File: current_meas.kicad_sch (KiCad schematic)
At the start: 33 parts, among them U23 LT3060ETS8-5#TRMPBF, U24 INA180A2IDBVR, U25 INA180A2IDBVR

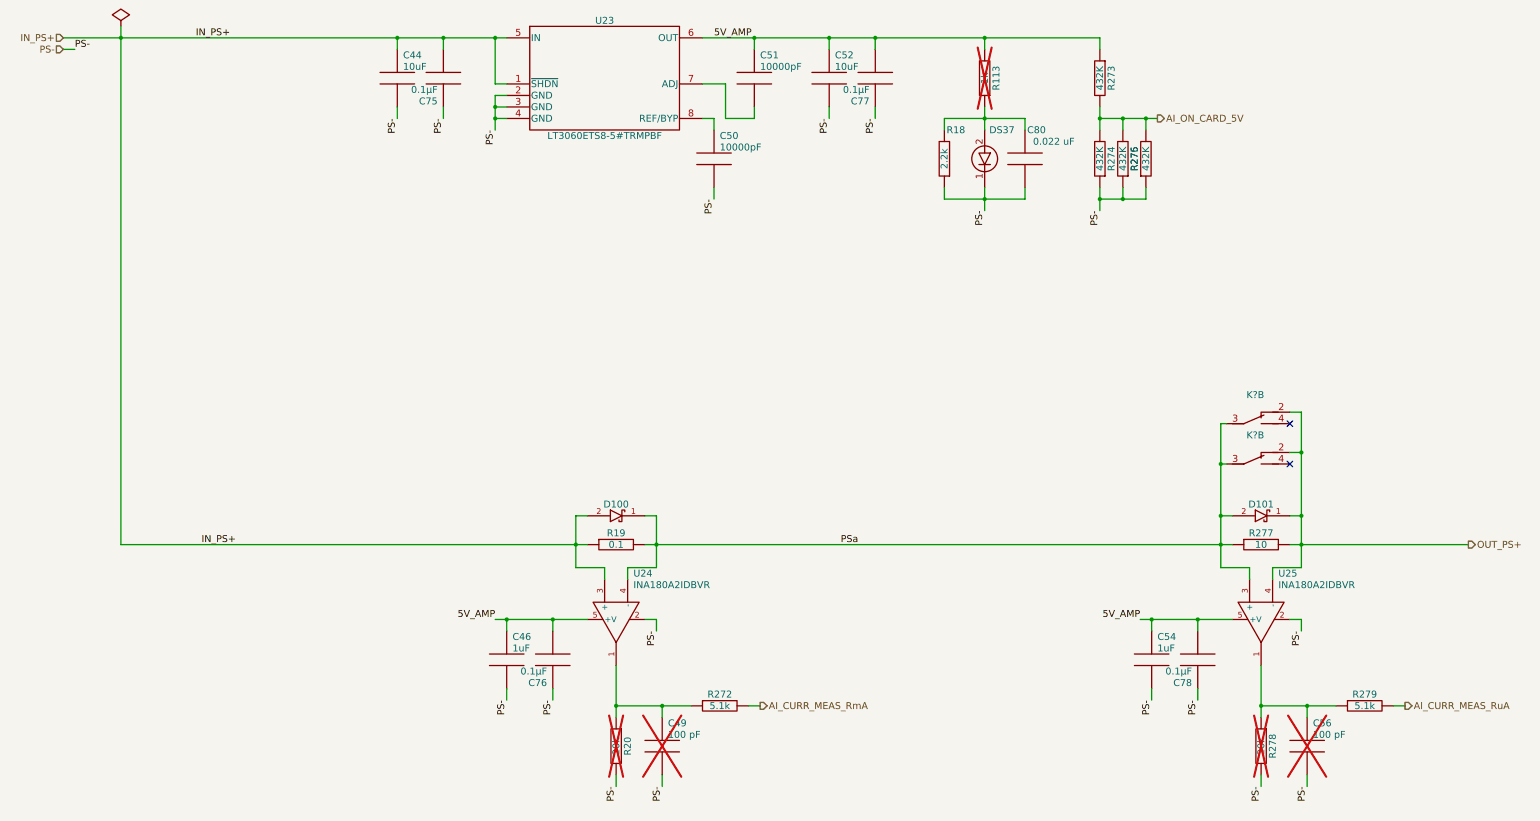
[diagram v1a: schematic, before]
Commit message: kicad 9 - r11-check gerber before sending to manufacturing
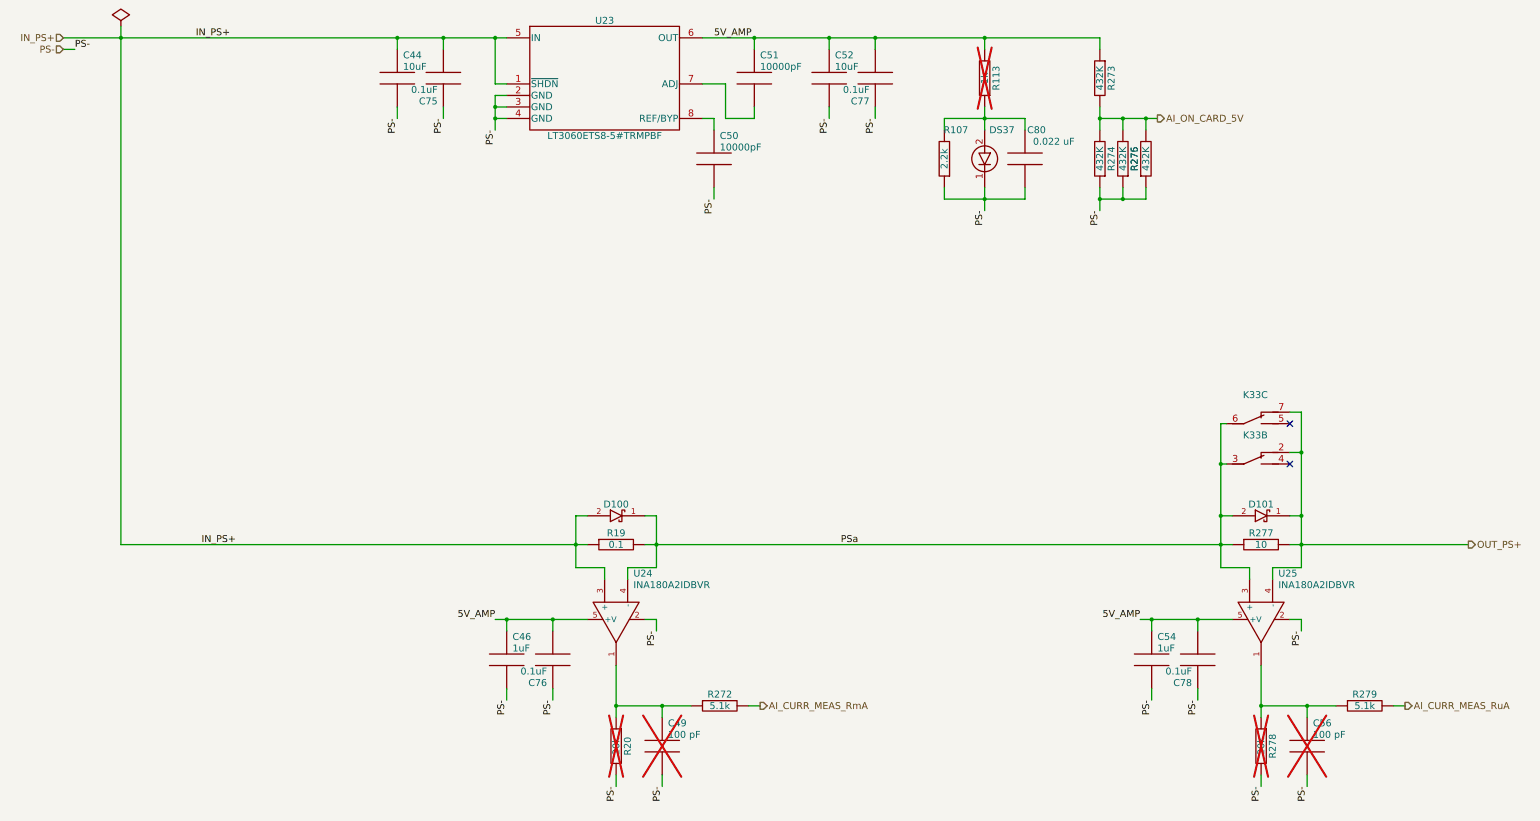
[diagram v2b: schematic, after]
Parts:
- C75, C76, C77, C78: Nominal 0.1µF -> 0.1uF
- gave numbers to parts that had none: 1
- renumbered R18 to R107
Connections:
- net OUT_PS+: now also K33.7; no longer K33.2
- net PSa: now also K33.6; no longer K33.3

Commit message: r11a - clean up mostly with reports naming, values, footprints and parts
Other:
- company: ARXTRON TECHNOLOGIES -> ${COMPANY}
- title: EOL ECU MIX CARD -> ${PART_NUM} ${PCB_NAME} ${ASSY_VARIANT} ${ASSY_NAME}
- moved on the sheet: U23
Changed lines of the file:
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@@
 	(paper "A3")
 	(title_block
-		(title "EOL ECU MIX CARD")
-		(date "2023-09-26")
-		(rev "0C")
-		(company "ARXTRON TECHNOLOGIES")
-		(comment 1 "A0180-V0")
-		(comment 2 "PRJ22180")
-		(comment 3 "EOL ECU RCM8 RCM9")
-		(comment 4 "ANTON TOKARSKYI")
+		(title "${PART_NUM} ${PCB_NAME} ${ASSY_VARIANT} ${ASSY_NAME}")
+		(date "2025-03-12")
+		(rev "${REVISION}${REVISION_SCH}")
+		(company "${COMPANY}")
+		(comment 1 "${PART_NUM}")
+		(comment 2 "${PRJ_NUM}")
+		(comment 3 "${PRJ_NAME}")
+		(comment 4 "${DESIGNED}")
+		(comment 5 "${PART_NUM_ICT}")
 	)
 	(junction
@@
 	(wire
 		(pts
-			(xy 180.34 59.69) (xy 182.88 59.69)
+			(xy 175.26 59.69) (xy 182.88 59.69)
 		)
 		(stroke
@@
 	(wire
 		(pts
-			(xy 180.34 41.91) (xy 191.77 41.91)
+			(xy 175.26 41.91) (xy 191.77 41.91)
 		)
 		(stroke
@@
 	(wire
 		(pts
-			(xy 137.16 52.07) (xy 134.62 52.07)
+			(xy 139.7 52.07) (xy 134.62 52.07)
 		)
 		(stroke
@@
 	(wire
 		(pts
-			(xy 134.62 41.91) (xy 137.16 41.91)
+			(xy 134.62 41.91) (xy 139.7 41.91)
 		)
 		(stroke
@@
 	(wire
 		(pts
-			(xy 134.62 59.69) (xy 137.16 59.69)
+			(xy 134.62 59.69) (xy 139.7 59.69)
 		)
 		(stroke
@@
 	(wire
 		(pts
-			(xy 180.34 52.07) (xy 185.42 52.07)
+			(xy 175.26 52.07) (xy 185.42 52.07)
 		)
 		(stroke
@@
 	(wire
 		(pts
-			(xy 137.16 54.61) (xy 134.62 54.61)
+			(xy 139.7 54.61) (xy 134.62 54.61)
 		)
 		(stroke
@@
 	(wire
 		(pts
-			(xy 134.62 57.15) (xy 137.16 57.15)
+			(xy 134.62 57.15) (xy 139.7 57.15)
 		)
 		(stroke
@@
 	(symbol
 		(lib_id "Analog_Devices:LT3060ETS8-5#TRMPBF")
-		(at 158.75 50.8 0)
+		(at 157.48 50.8 0)
 		(unit 1)
 		(exclude_from_sim no)
@@
 		(dnp no)
 		(property "Reference" "U23"
-			(at 158.75 38.1 0)
+			(at 157.48 38.1 0)
 			(effects
 				(font
@@
 		)
 		(property "Value" "LT3060ETS8-5#TRMPBF"
-			(at 158.75 66.04 0)
+			(at 157.48 66.04 0)
 			(effects
 				(font
@@
 		)
 		(property "Footprint" "_AnalogDevices:SOT65P280X100-8"
-			(at 158.75 81.28 0)
+			(at 157.48 81.28 0)
 			(effects
 				(font
@@
 		)
 		(property "Datasheet" ""
-			(at 148.59 46.99 0)
+			(at 147.32 46.99 0)
 			(effects
 				(font
@@
 		)
 		(property "Description" "IC REG LINEAR 5V 100MA TSOT23-8"
-			(at 158.75 73.66 0)
+			(at 157.48 73.66 0)
 			(effects
 				(font
@@
 		)
 		(property "SupplierDevicePackage" "TSOT-23-8"
-			(at 158.75 76.2 0)
+			(at 157.48 76.2 0)
 			(effects
 				(font
@@
 		)
 		(property "SupplierPartNumber" "LT3060ETS8-5#TRMPBFTR-ND"
-			(at 158.75 68.58 0)
+			(at 157.48 68.58 0)
 			(effects
 				(font
@@
 		)
 		(property "Supplier" "Digi-Key"
-			(at 158.75 78.74 0)
+			(at 157.48 78.74 0)
 			(effects
 				(font
@@
 		)
 		(property "ManufacturerPartNumber" "LT3060ETS8-5#TRMPBF"
-			(at 158.75 63.5 0)
+			(at 157.48 63.5 0)
 			(effects
 				(font
@@
 		)
 		(property "Manufacturer" "Analog Devices Inc."
-			(at 158.75 71.12 0)
+			(at 157.48 71.12 0)
 			(effects
 				(font
